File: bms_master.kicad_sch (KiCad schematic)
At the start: 90 parts, among them J1 Conn_01x02, J2 Conn_01x02, J3 Conn_01x02, J4 Conn_01x04, J5 Conn_01x04, J6 Conn_01x06, Q1 PMV15ENE, Q2 PMV74EPE, Q3 PMV74EPE, SW1 SW_Push, U1 TPS7B88, U2 MCP1700x-330xxMB, U3 STM32F103C8Tx, U4 SN65HVD1050D, U5 M24C64-R, U6 MAX6126, U7 MAX11163, U8 741G3157, U9 TPS25961, Y1 8M

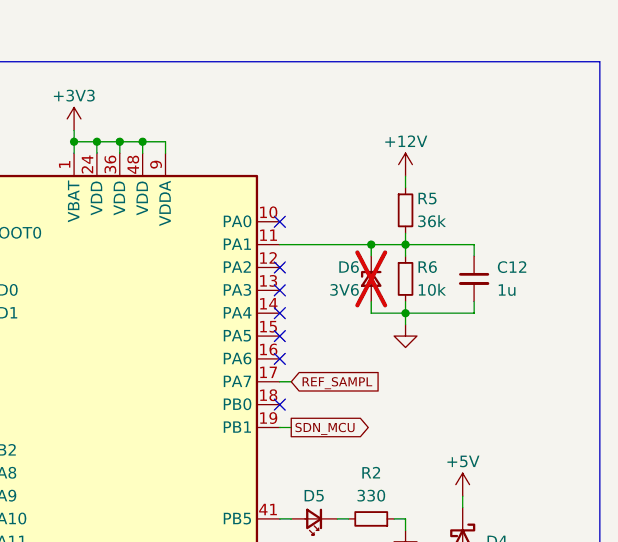
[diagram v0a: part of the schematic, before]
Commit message: *: Update 12 volt rail measurement circuit
Select a zener and increase the upper resistor slightly.
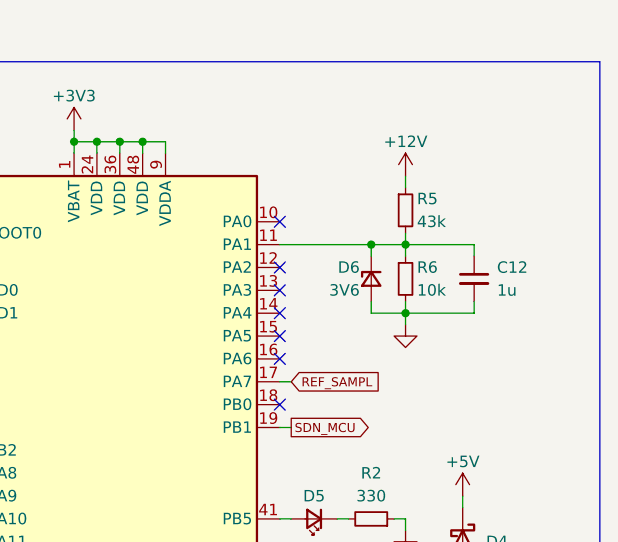
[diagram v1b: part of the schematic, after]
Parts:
- D6: Dist (none) -> LCSC; Dist # (none) -> C3739733; Mfr (none) -> VISHAY; Mfr # (none) -> BZX384C3V6; now fitted
- R5: value 36k -> 43k
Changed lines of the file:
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@@
 		(in_bom yes)
 		(on_board yes)
-		(dnp yes)
+		(dnp no)
 		(property "Reference" "D6"
 			(at 255.27 40.64 90)
@@
 		(property "Description" "Zener diode, small symbol"
 			(at 256.54 41.91 0)
+			(effects
+				(font
+					(size 1.27 1.27)
+				)
+				(hide yes)
+			)
+		)
+		(property "Dist" "LCSC"
+			(at 256.54 41.91 90)
+			(effects
+				(font
+					(size 1.27 1.27)
+				)
+				(hide yes)
+			)
+		)
+		(property "Dist #" "C3739733"
+			(at 256.54 41.91 90)
+			(effects
+				(font
+					(size 1.27 1.27)
+				)
+				(hide yes)
+			)
+		)
+		(property "Mfr" "VISHAY"
+			(at 256.54 41.91 90)
+			(effects
+				(font
+					(size 1.27 1.27)
+				)
+				(hide yes)
+			)
+		)
+		(property "Mfr #" "BZX384C3V6"
+			(at 256.54 41.91 90)
 			(effects
 				(font
@@
 			)
 		)
-		(property "Value" "36k"
+		(property "Value" "43k"
 			(at 261.62 35.56 0)
 			(effects

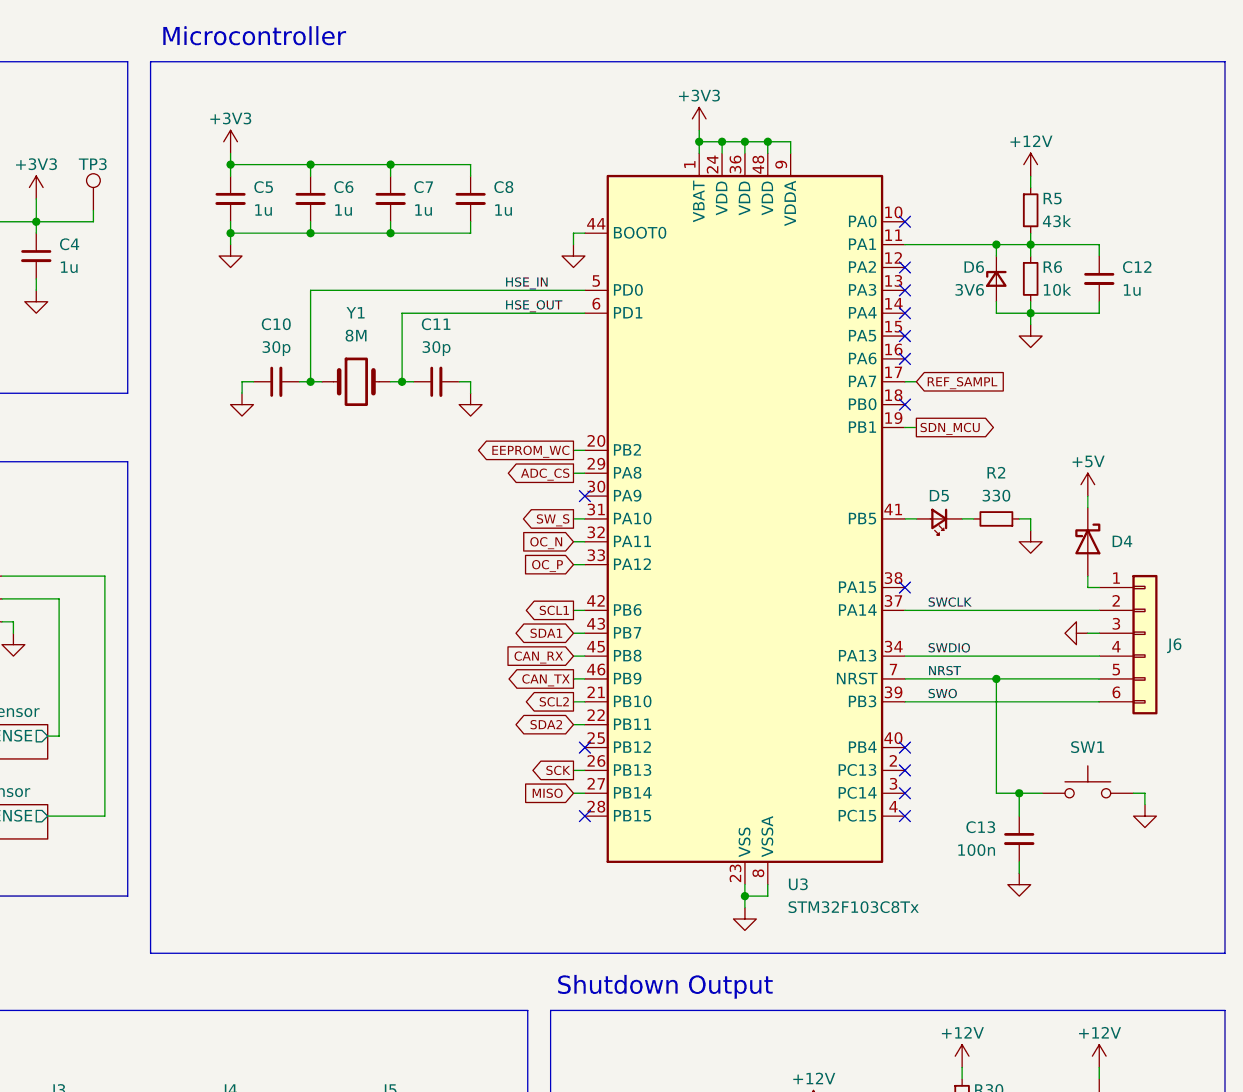
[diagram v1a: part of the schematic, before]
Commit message: *: Add TPS3851 watchdog IC
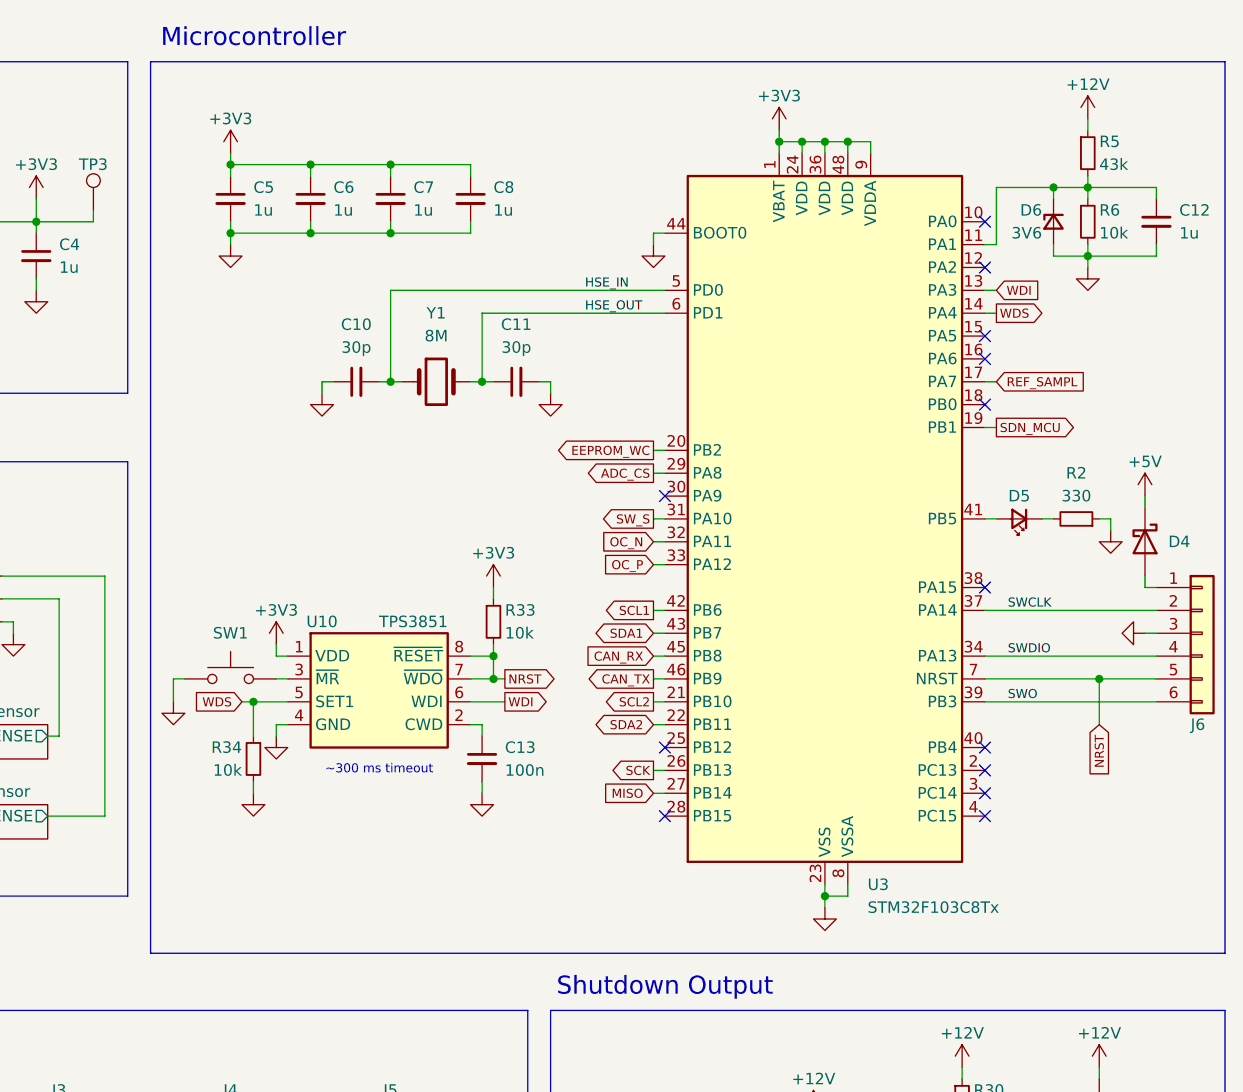
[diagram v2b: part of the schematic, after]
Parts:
- added R33, R34: 10k, Resistor_SMD:R_0603_1608Metric, symbol Device:R_Small
- added U10: TPS3851, Package_SON:VSON-8-1EP_3x3mm_P0.65mm_EP1.6x2.4mm, symbol yfs:TPS3851
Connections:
- net +3V3: now also R33.1, U10.1 (VDD)
- net GND: now also SW1.1, R34.2, U10.4 (GND), U10.9 (GND); no longer SW1.2
- net NRST: now also R33.2, U10.7 (~{WDO}), U10.8 (~{RESET}); no longer C13.1, SW1.1
- net WDI: now reaches U3.13 (PA3)
- net WDI: now also U10.6 (WDI)
- net WDS: now reaches U3.14 (PA4)
- net WDS: now also R34.1, U10.5 (SET1)
- new net: C13.1, U10.2 (CWD)
- new net: SW1.2, U10.3 (~{MR})
- no-connect marks 16 -> 14
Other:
- note added: "~300 ms timeout"
- moved on the sheet: C10, C11, C12, C13, D4, D5, D6, J6, R2, R5, R6, SW1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

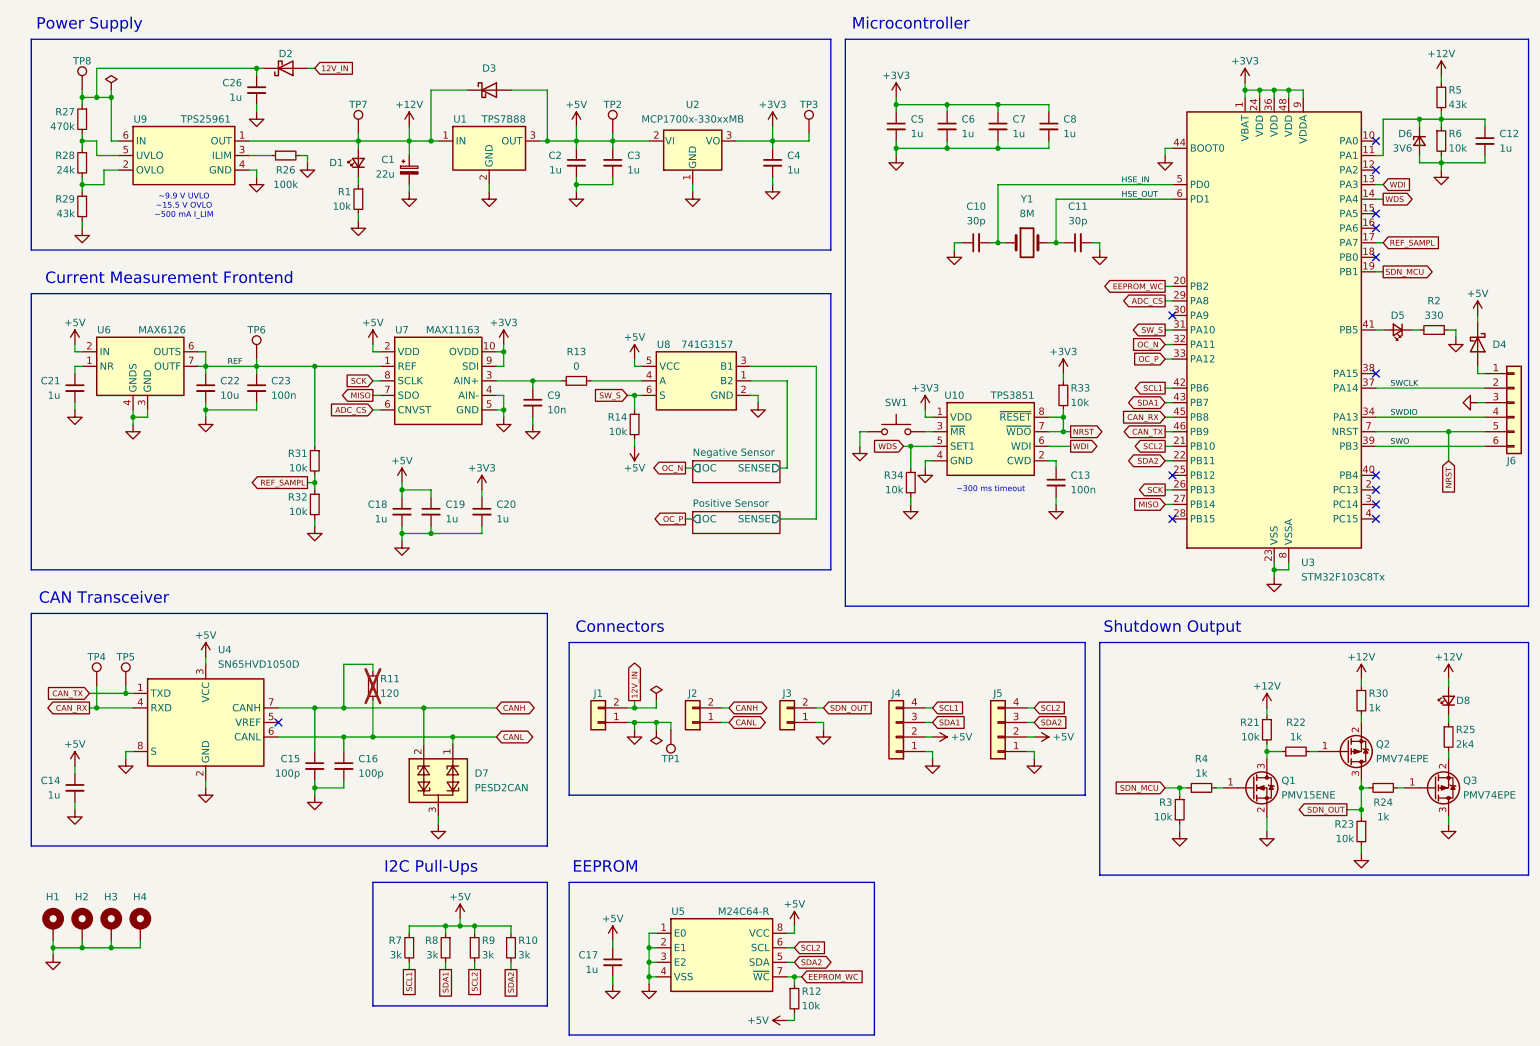
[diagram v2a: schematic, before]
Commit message: *: Reorder reference designators
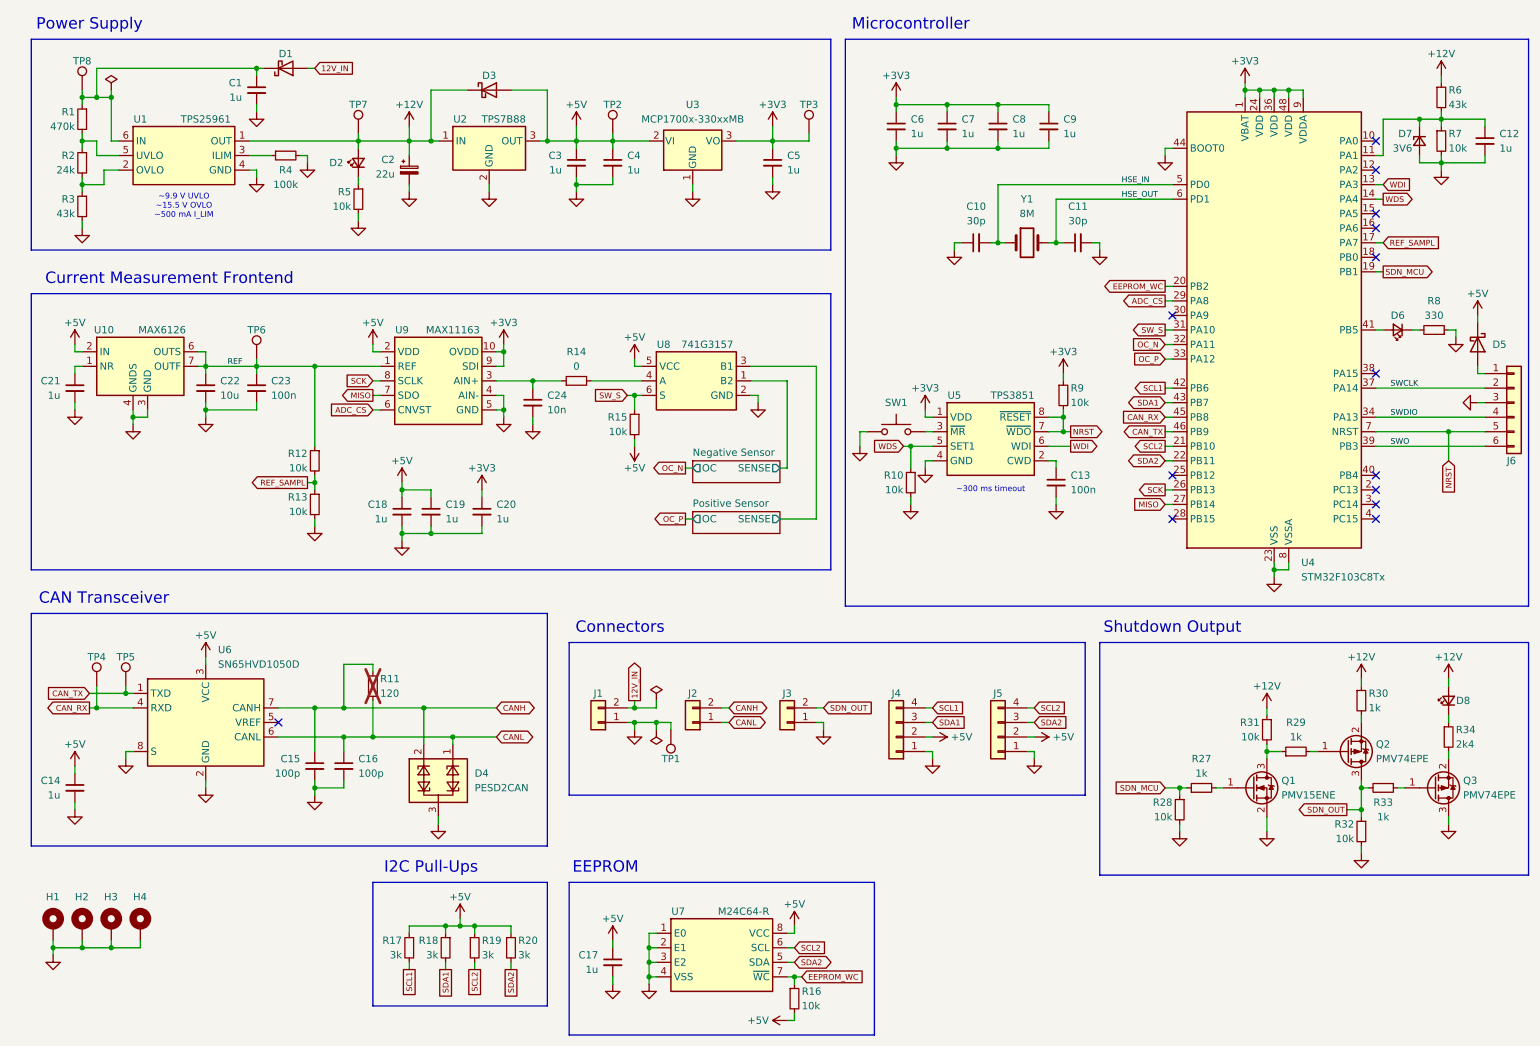
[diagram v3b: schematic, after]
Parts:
- renumbered C26 to C1, C1 to C2, C9 to C24, C2 to C3, C3 to C4, C4 to C5, C5 to C6, C6 to C7, C7 to C8, C8 to C9, D2 to D1, D1 to D2, D7 to D4, D4 to D5, D5 to D6, D6 to D7, R27 to R1, R34 to R10, R31 to R12, R32 to R13, R13 to R14, R14 to R15, R12 to R16, R7 to R17, R8 to R18, R9 to R19, R28 to R2, R10 to R20, R4 to R27, R3 to R28, R22 to R29, R29 to R3, R21 to R31, R23 to R32, R24 to R33, R25 to R34, R26 to R4, R1 to R5, R5 to R6, R6 to R7, R2 to R8, R33 to R9, U9 to U1, U6 to U10, U1 to U2, U2 to U3, U3 to U4, U10 to U5, U4 to U6, U5 to U7, U7 to U9

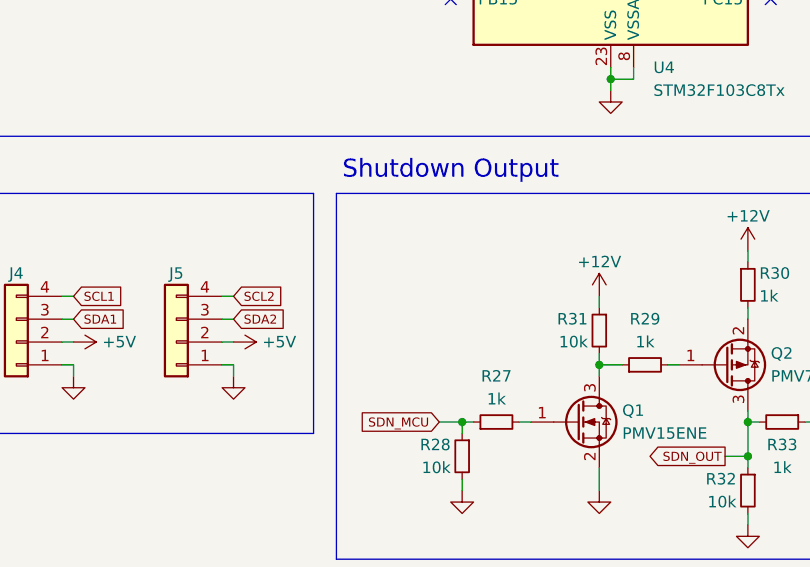
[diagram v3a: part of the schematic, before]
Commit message: *: Add shutdown test point
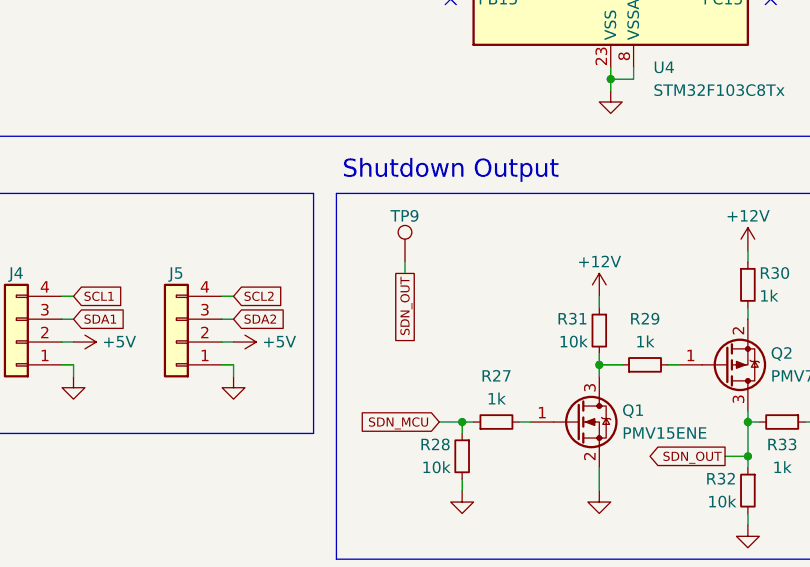
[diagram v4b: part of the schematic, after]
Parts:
- added TP9: TestPoint, TestPoint:TestPoint_Keystone_5000-5004_Miniature, symbol Connector:TestPoint
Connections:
- net SDN_OUT: now also TP9.1
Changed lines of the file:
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@@
 	(wire
 		(pts
+			(xy 214.63 130.81) (xy 214.63 132.08)
+		)
+		(stroke
+			(width 0)
+			(type default)
+		)
+	)
+	(wire
+		(pts
 			(xy 86.36 35.56) (xy 86.36 38.1)
 		)
@@
 		)
 	)
+	(global_label "SDN_OUT"
+		(shape passive)
+		(at 214.63 132.08 270)
+		(fields_autoplaced yes)
+		(effects
+			(font
+				(size 1 1)
+			)
+			(justify right)
+		)
+		(property "Intersheetrefs" "${INTERSHEET_REFS}"
+			(at 214.63 140.1743 90)
+			(effects
+				(font
+					(size 1.27 1.27)
+				)
+				(justify right)
+				(hide yes)
+			)
+		)
+	)
 	(global_label "SDN_MCU"
 		(shape output)
@@
 					(unit 1)
 				)
+			)
+		)
+	)
+	(symbol
+		(lib_id "Connector:TestPoint")
+		(at 214.63 130.81 0)
+		(unit 1)
+		(exclude_from_sim no)
+		(in_bom yes)
+		(on_board yes)
+		(dnp no)
+		(property "Reference" "TP9"
+			(at 214.63 125.73 0)
+			(effects
+				(font
+					(size 1.27 1.27)
+				)
+			)
+		)
+		(property "Value" "TestPoint"
+			(at 217.17 128.7779 0)
+			(effects
+				(font
+					(size 1.27 1.27)
+				)
+				(justify left)
+				(hide yes)
+			)
+		)
+		(property "Footprint" "TestPoint:TestPoint_Keystone_5000-5004_Miniature"
+			(at 219.71 130.81 0)
+			(effects
+				(font
+					(size 1.27 1.27)
+				)
+				(hide yes)
+			)
+		)
+		(property "Datasheet" "~"
+			(at 219.71 130.81 0)
+			(effects
+				(font
+					(size 1.27 1.27)
+				)
+				(hide yes)
+			)
+		)
+		(property "Description" "test point"
+			(at 214.63 130.81 0)
+			(effects
+				(font
+					(size 1.27 1.27)
+				)
+				(hide yes)
+			)
+		)
+		(pin "1"
+		)
+		(instances
+			(project "bms_master"
+				(path "/ff788b45-a486-492a-a3f3-4e15ca08a026"
+					(reference "TP9")
+					(unit 1)
+				)
